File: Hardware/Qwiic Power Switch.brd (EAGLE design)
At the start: 25.4 x 25.4 mm, 67 parts, among them J1 Qwiic Right Angle, J2 PTH, J3 Qwiic Right Angle, J4 PTH, Q1 20V/4.2A/52mΩ/1.4W, U1 74HC1G04, U2 PCA9536

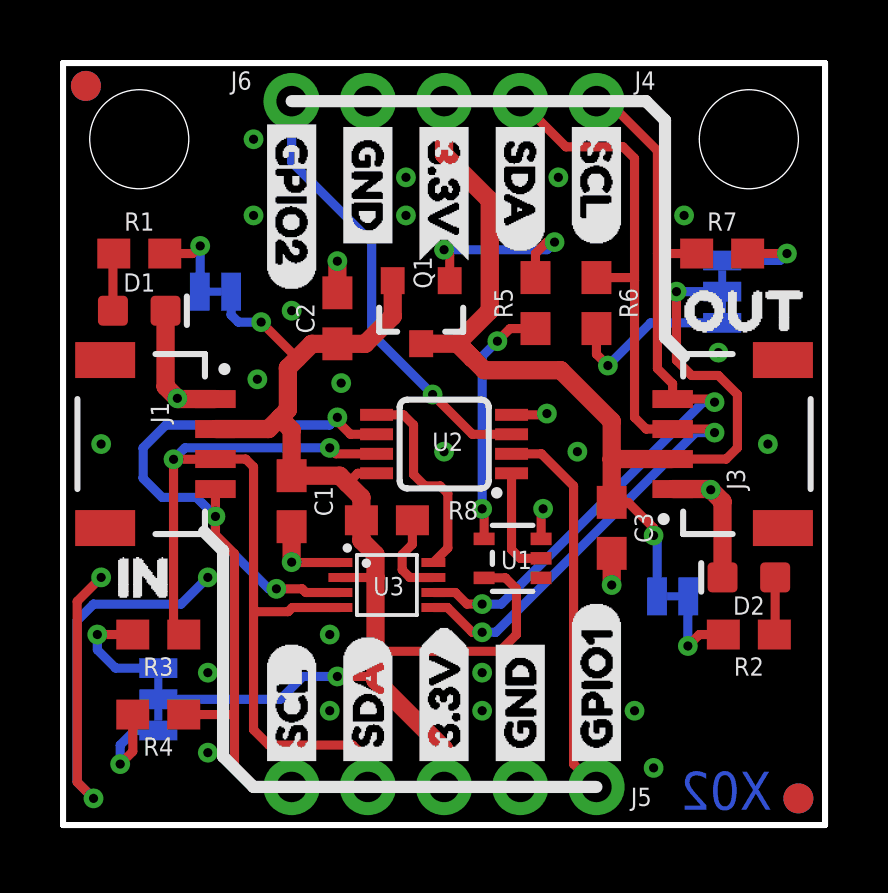
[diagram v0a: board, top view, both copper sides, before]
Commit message: Remove New_Parts.lbr
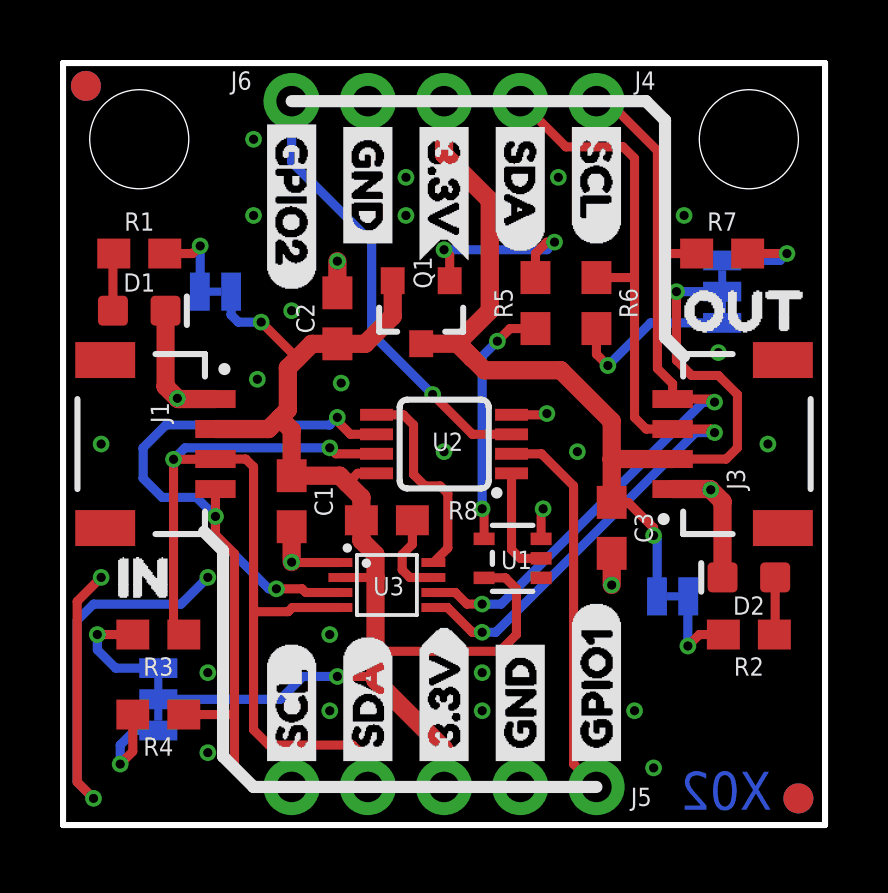
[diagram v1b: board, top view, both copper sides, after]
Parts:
- U$34: device Switch:SWITCH0 -> switch:SWITCH0
- U2: device New_Parts:MSOP8 -> SparkFun-IC-Conversion:MSOP8
